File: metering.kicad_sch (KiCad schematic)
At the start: 6 parts, among them J1 Electric Meter IR TTL, J2 Gas Meter Reed Contact, U1 NodeMCU v2

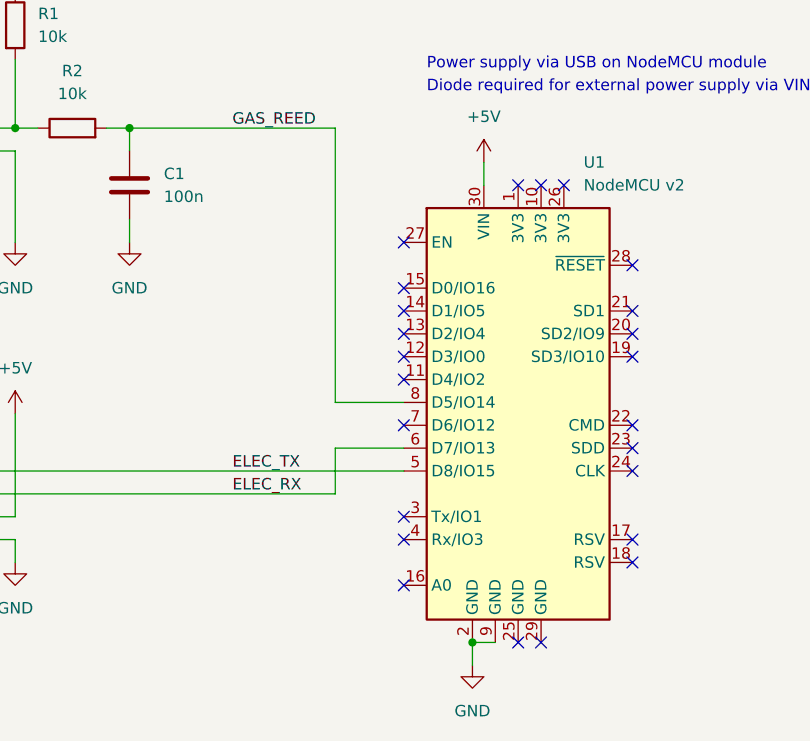
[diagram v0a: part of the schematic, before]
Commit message: Update power symbols, add power flags to satisfy ERC
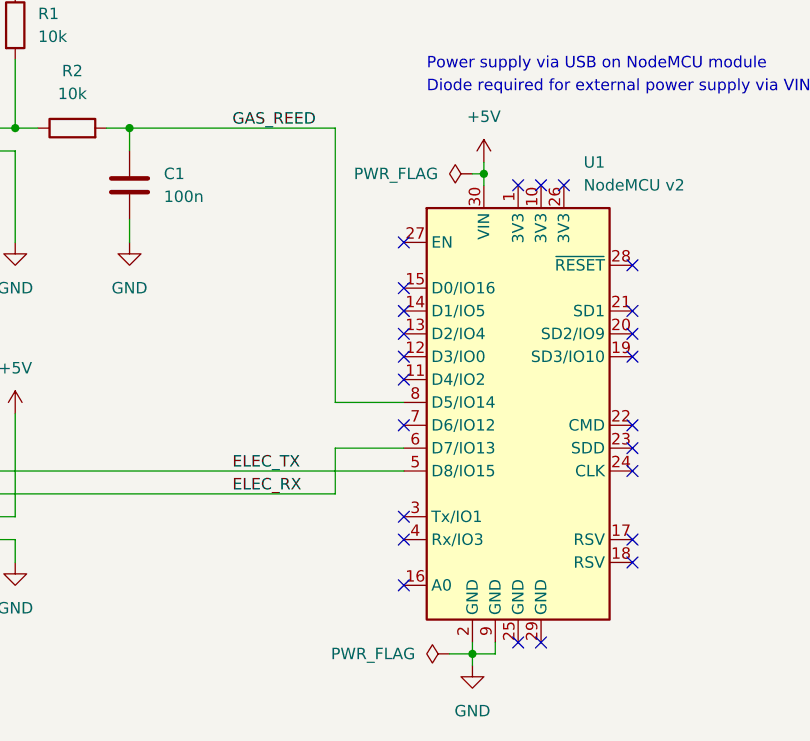
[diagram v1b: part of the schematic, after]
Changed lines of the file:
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@@
+	)
+	(junction
+		(at 139.7 109.22)
+		(diameter 0)
+		(color 0 0 0 0)
+	)
+	(junction
+		(at 140.97 55.88)
+		(diameter 0)
+		(color 0 0 0 0)
 	)
 	(junction
@@
 		(color 0 0 0 0)
 	)
-	(junction
-		(at 139.7 107.95)
-		(diameter 0)
-		(color 0 0 0 0)
-	)
 	(no_connect
 		(at 132.08 76.2)
@@
 	(wire
 		(pts
+			(xy 139.7 109.22) (xy 139.7 107.95)
+		)
+		(stroke
+			(width 0)
+			(type default)
+		)
+	)
+	(wire
+		(pts
 			(xy 88.9 50.8) (xy 91.44 50.8)
 		)
@@
 	(wire
 		(pts
+			(xy 139.7 109.22) (xy 139.7 110.49)
+		)
+		(stroke
+			(width 0)
+			(type default)
+		)
+	)
+	(wire
+		(pts
 			(xy 88.9 33.02) (xy 88.9 35.56)
 		)
@@
 	(wire
 		(pts
+			(xy 137.16 109.22) (xy 139.7 109.22)
+		)
+		(stroke
+			(width 0)
+			(type default)
+		)
+	)
+	(wire
+		(pts
 			(xy 81.28 50.8) (xy 88.9 50.8)
 		)
@@
 	(wire
 		(pts
+			(xy 142.24 109.22) (xy 142.24 107.95)
+		)
+		(stroke
+			(width 0)
+			(type default)
+		)
+	)
+	(wire
+		(pts
 			(xy 88.9 43.18) (xy 88.9 50.8)
 		)
@@
 	(wire
 		(pts
-			(xy 140.97 57.15) (xy 140.97 54.61)
+			(xy 140.97 55.88) (xy 140.97 54.61)
+		)
+		(stroke
+			(width 0)
+			(type default)
+		)
+	)
+	(wire
+		(pts
+			(xy 140.97 57.15) (xy 140.97 55.88)
 		)
 		(stroke
@@
 	(wire
 		(pts
-			(xy 139.7 107.95) (xy 139.7 110.49)
-		)
-		(stroke
-			(width 0)
-			(type default)
-		)
-	)
-	(wire
-		(pts
 			(xy 88.9 53.34) (xy 81.28 53.34)
 		)
@@
 	(wire
 		(pts
-			(xy 139.7 107.95) (xy 142.24 107.95)
+			(xy 139.7 55.88) (xy 140.97 55.88)
+		)
+		(stroke
+			(width 0)
+			(type default)
+		)
+	)
+	(wire
+		(pts
+			(xy 139.7 109.22) (xy 142.24 109.22)
 		)
 		(stroke
@@
 			)
 			(justify left bottom)
+		)
+	)
+	(symbol
+		(lib_id "power:PWR_FLAG")
+		(at 139.7 55.88 90)
+		(unit 1)
+		(exclude_from_sim no)
+		(in_bom yes)
+		(on_board yes)
+		(dnp no)
+		(fields_autoplaced yes)
+		(property "Reference" "#FLG01"
+			(at 137.795 55.88 0)
+			(effects
+				(font
+					(size 1.27 1.27)
+				)
+				(hide yes)
+			)
+		)
+		(property "Value" "PWR_FLAG"
+			(at 135.89 55.8799 90)
+			(effects
+				(font
+					(size 1.27 1.27)
+				)
+				(justify left)
+			)
+		)
+		(property "Footprint" ""
+			(at 139.7 55.88 0)
+			(effects
+				(font
+					(size 1.27 1.27)
+				)
+				(hide yes)
+			)
+		)
+		(property "Datasheet" "~"
+			(at 139.7 55.88 0)
+			(effects
+				(font
+					(size 1.27 1.27)
+				)
+				(hide yes)
+			)
+		)
+		(property "Description" "Special symbol for telling ERC where power comes from"
+			(at 139.7 55.88 0)
+			(effects
+				(font
+					(size 1.27 1.27)
+				)
+				(hide yes)
+			)
+		)
+		(pin "1"
+		)
+		(instances
+			(project ""
+				(path "/2132c704-8b90-4a68-a04d-0b4be367d67b"
+					(reference "#FLG01")
+					(unit 1)
+				)
+			)
 		)
 	)
@@
 			)
 		)
-		(property "Description" ""
+		(property "Description" "Power symbol creates a global label with name \"+5V\""
 			(at 140.97 54.61 0)
 			(effects
@@
 			)
 		)
-		(property "Description" ""
+		(property "Description" "Power symbol creates a global label with name \"GND\" , ground"
 			(at 139.7 110.49 0)
 			(effects
@@
 	)
 	(symbol
+		(lib_id "power:PWR_FLAG")
+		(at 137.16 109.22 90)
+		(unit 1)
+		(exclude_from_sim no)
+		(in_bom yes)
+		(on_board yes)
+		(dnp no)
+		(fields_autoplaced yes)
+		(property "Reference" "#FLG02"
+			(at 135.255 109.22 0)
+			(effects
+				(font
+					(size 1.27 1.27)
+				)
+				(hide yes)
+			)
+		)
+		(property "Value" "PWR_FLAG"
+			(at 133.35 109.2199 90)
+			(effects
+				(font
+					(size 1.27 1.27)
+				)
+				(justify left)
+			)
+		)
+		(property "Footprint" ""
+			(at 137.16 109.22 0)
+			(effects
+				(font
+					(size 1.27 1.27)
+				)
+				(hide yes)
+			)
+		)
+		(property "Datasheet" "~"
+			(at 137.16 109.22 0)
+			(effects
+				(font
+					(size 1.27 1.27)
+				)
+				(hide yes)
+			)
+		)
+		(property "Description" "Special symbol for telling ERC where power comes from"
+			(at 137.16 109.22 0)
+			(effects
+				(font
+					(size 1.27 1.27)
+				)
+				(hide yes)
+			)
+		)
+		(pin "1"
+		)
+		(instances
+			(project "metering"
+				(path "/2132c704-8b90-4a68-a04d-0b4be367d67b"
+					(reference "#FLG02")
+					(unit 1)
+				)
+			)
+		)
+	)
+	(symbol
 		(lib_id "power:GND")
 		(at 88.9 63.5 0)
@@
 			)
 		)
-		(property "Description" ""
+		(property "Description" "Power symbol creates a global label with name \"GND\" , ground"
 			(at 88.9 63.5 0)
 			(effects
@@
 			)
 		)
-		(property "Description" ""
+		(property "Description" "Power symbol creates a global label with name \"+5V\""
 			(at 88.9 33.02 0)
 			(effects
@@
 			)
 		)
-		(property "Description" ""
+		(property "Description" "Power symbol creates a global label with name \"GND\" , ground"
 			(at 88.9 99.06 0)
 			(effects
@@
 			)
 		)
-		(property "Description" ""
+		(property "Description" "Power symbol creates a global label with name \"GND\" , ground"
 			(at 101.6 63.5 0)
 			(effects
@@
 			)
 		)
-		(property "Description" ""
+		(property "Description" "Power symbol creates a global label with name \"+5V\""
 			(at 88.9 82.55 0)
 			(effects

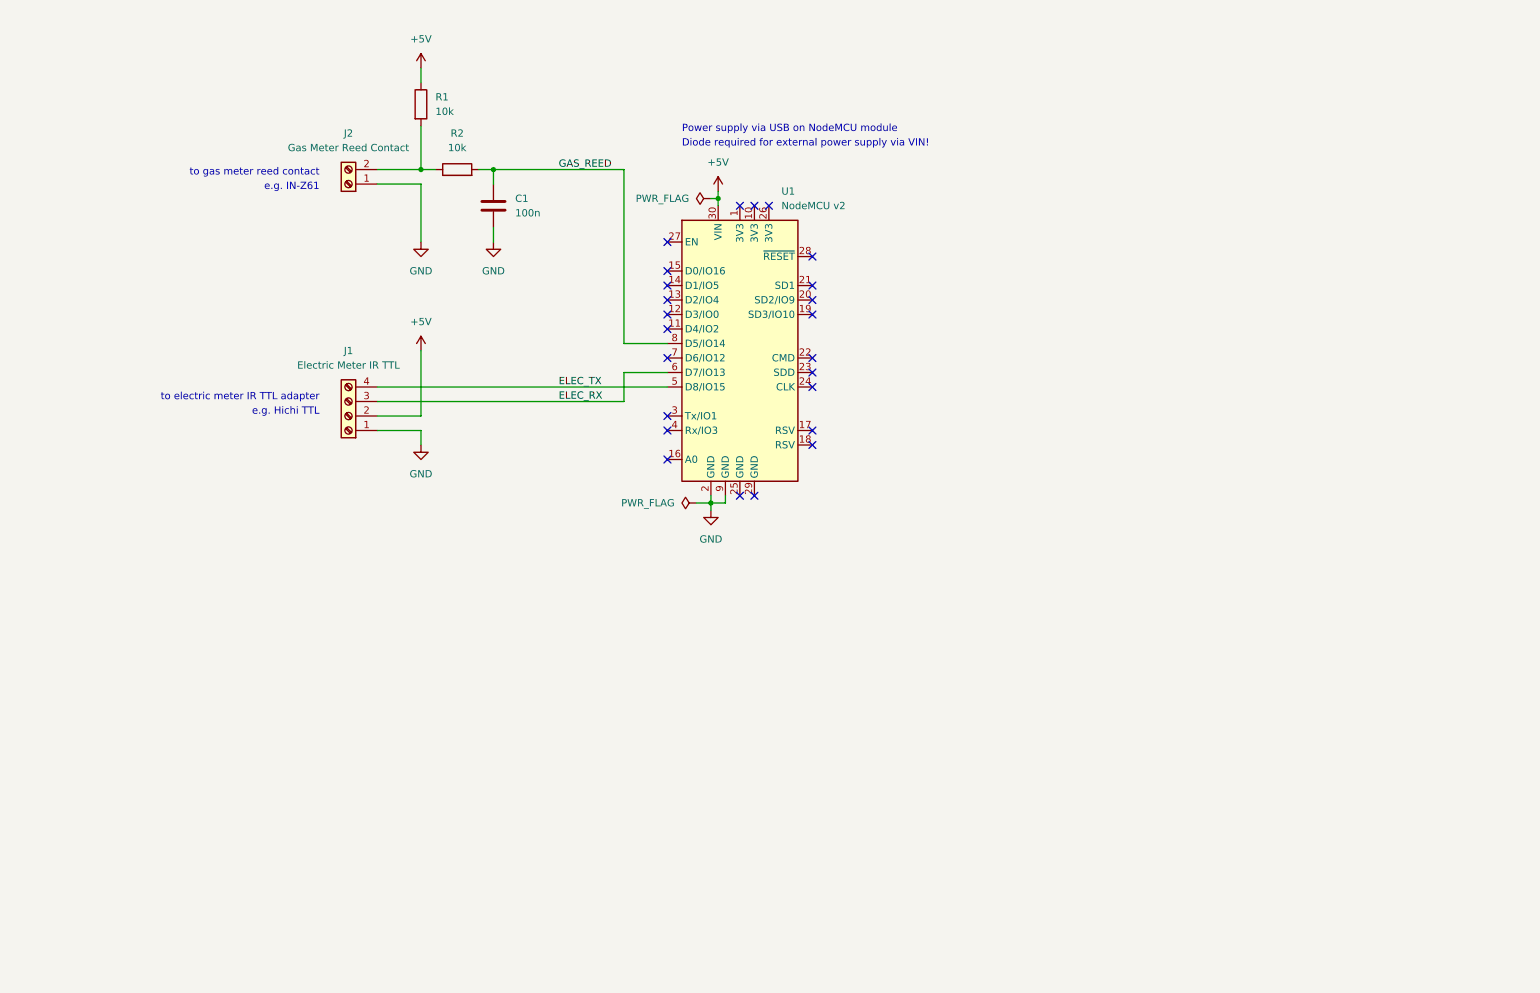
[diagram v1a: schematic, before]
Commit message: Recreate schematic with ESP32-C3-WROOM module and hardware debounce
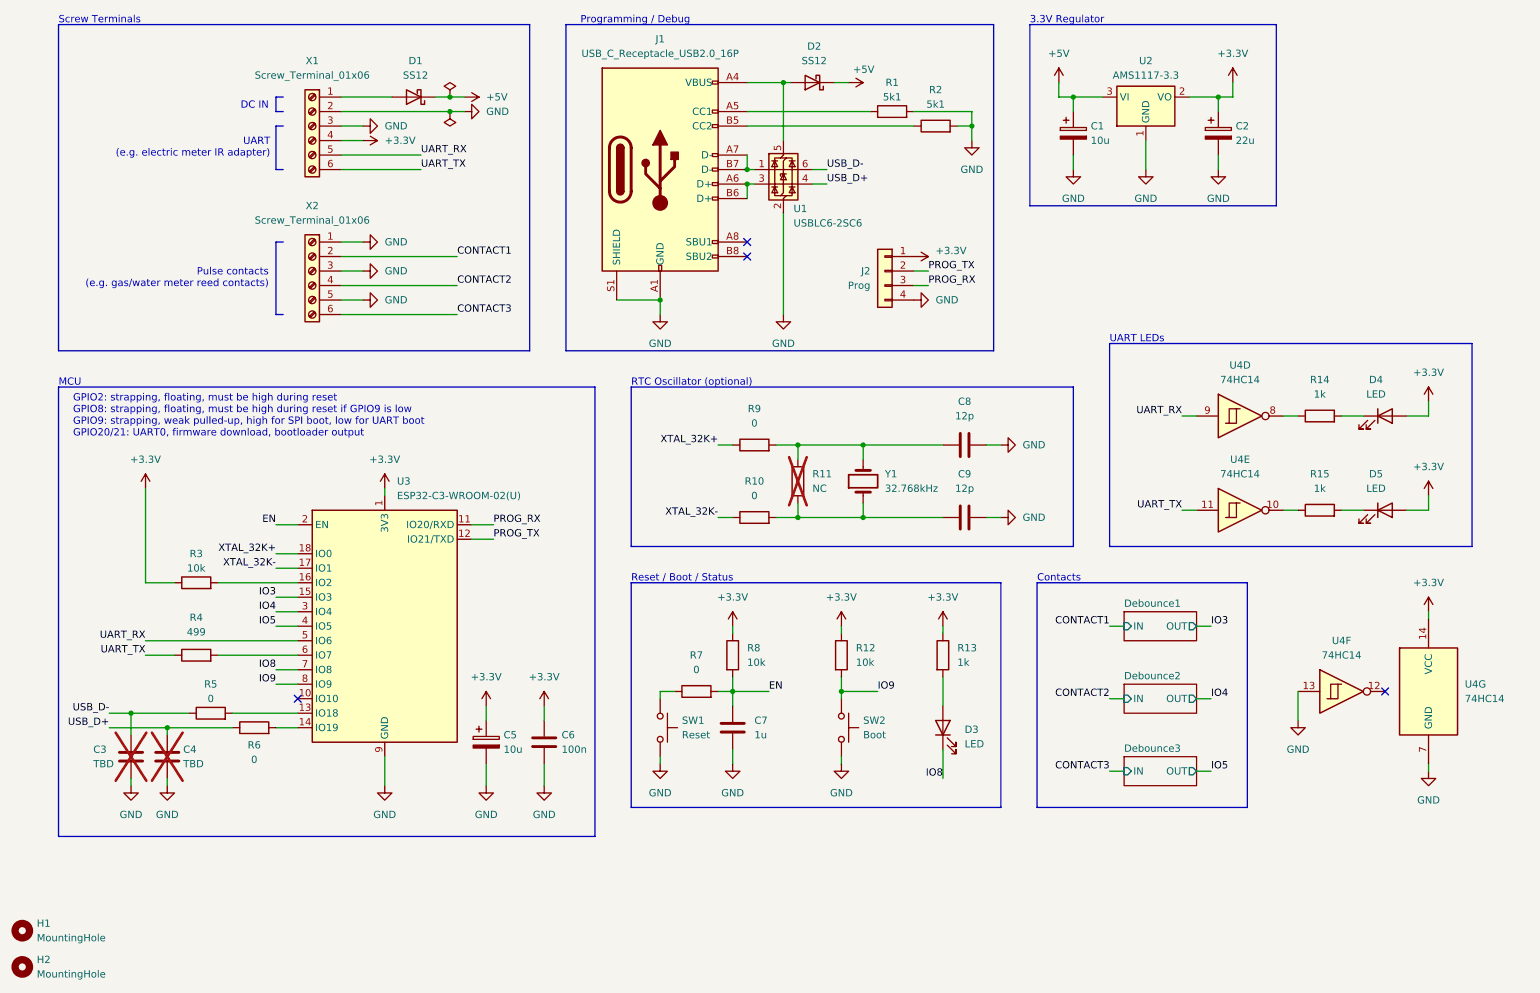
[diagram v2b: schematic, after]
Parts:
- removed C1: 100n, symbol Device:C
- removed J1: Electric Meter IR TTL, Connector_PinSocket_2.54mm:PinSocket_1x04_P2.54mm_Vertical, symbol Connector:Screw_Terminal_01x04
- removed J2: Gas Meter Reed Contact, Connector_PinSocket_2.54mm:PinSocket_1x02_P2.54mm_Vertical, symbol Connector:Screw_Terminal_01x02
- removed U1: NodeMCU v2, NodeMCU_v2:NodeMCU_v2, symbol NodeMCU_v2:NodeMCU_v2
- added C1, C5: 10u, Capacitor_Tantalum_SMD:CP_EIA-3216-18_Kemet-A, symbol Device:C_Polarized
- added C2: 22u, Capacitor_Tantalum_SMD:CP_EIA-3216-18_Kemet-A, symbol Device:C_Polarized
- added C3, C4: TBD, Capacitor_SMD:C_0805_2012Metric, symbol Device:C
- added C6: 100n, Capacitor_SMD:C_0805_2012Metric, symbol Device:C
- added C7: 1u, Capacitor_SMD:C_0805_2012Metric, symbol Device:C
- added C8, C9: 12p, Capacitor_SMD:C_0805_2012Metric, symbol Device:C
- added D1, D2: SS12, Diode_SMD:D_SMA, symbol Diode:SS12
- added D3, D4, D5: LED, LED_THT:LED_D3.0mm_Horizontal_O6.35mm_Z2.0mm, symbol Device:LED
- added H1, H2: MountingHole, MountingHole:MountingHole_3.2mm_M3, symbol Mechanical:MountingHole
- added J1: USB_C_Receptacle_USB2.0_16P, Connector_USB:USB_C_Receptacle_GCT_USB4110, symbol Connector:USB_C_Receptacle_USB2.0_16P
- added J2: Prog, Connector_PinHeader_2.54mm:PinHeader_1x04_P2.54mm_Vertical, symbol Connector_Generic:Conn_01x04
- added R10, R5, R6, R7, R9: 0, Resistor_SMD:R_0805_2012Metric, symbol Device:R
- added R11: NC, Resistor_SMD:R_0805_2012Metric, symbol Device:R
- added R12, R3, R8: 10k, Resistor_SMD:R_0805_2012Metric, symbol Device:R
- added R13, R14, R15: 1k, Resistor_SMD:R_0805_2012Metric, symbol Device:R
- added R4: 499, Resistor_SMD:R_0805_2012Metric, symbol Device:R
- added SW1: Reset, Button_Switch_SMD:SW_SPST_PTS647_Sx38, symbol Switch:SW_Push
- added SW2: Boot, Button_Switch_SMD:SW_SPST_PTS647_Sx38, symbol Switch:SW_Push
- added U1: USBLC6-2SC6, Package_TO_SOT_SMD:SOT-23-6, symbol Power_Protection:USBLC6-2SC6
- added U2: AMS1117-3.3, Package_TO_SOT_SMD:SOT-223-3_TabPin2, symbol Regulator_Linear:AMS1117-3.3
- added U3: ESP32-C3-WROOM-02(U), RF_Module:ESP32-C3-WROOM-02, symbol RF_Module:ESP32-C3-WROOM-02
- added U4: 74HC14, Package_SO:SOIC-14_3.9x8.7mm_P1.27mm, symbol 74xx:74HC14
- added X1, X2: Screw_Terminal_01x06, TerminalBlock_Phoenix:TerminalBlock_Phoenix_MKDS-1,5-6-5.08_1x06_P5.08mm_Horizontal, symbol Connector:Screw_Terminal_01x06
- added Y1: 32.768kHz, Crystal:Crystal_SMD_3215-2Pin_3.2x1.5mm, symbol Device:Crystal
- R1, R2: value 10k -> 5k1; footprint (none) -> Resistor_SMD:R_0805_2012Metric
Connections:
- net GAS_REED is gone; now on net GND: R2.2
- net +5V: now also C1.1, D1.1 (K), D2.1 (K), U2.3 (VI); no longer R1.1
- net GND: now also R1.2, C1.2, C2.2, C3.2, C4.2, C5.2, C6.2, C7.2, C8.2, C9.2, J1.A1 (GND), J1.A12 (GND), J1.B1 (GND), J1.B12 (GND), J1.S1 (SHIELD), J2.4 (Pin_4), SW1.2, SW2.2, U1.2 (GND), U2.1 (GND), U3.19 (GND), U3.9 (GND), U4.13, U4.7 (GND), X1.2 (Pin_2), X1.3 (Pin_3), X2.1 (Pin_1), X2.3 (Pin_3), X2.5 (Pin_5)
- net at R2.1: now also J1.B5 (CC2); no longer R1.2
- new net: R14.1, U4.8
- new net: R7.1, SW1.1
- new net: R15.1, U4.10
- new net: C8.1, R11.2, R9.2, Y1.2
- new net: R3.2, U3.16 (IO2)
- new net: R6.2, U3.14 (IO19)
- new net: C9.1, R10.2, R11.1, Y1.1
- new net: D3.2 (A), R13.2
- new net: J1.A5 (CC1), R1.1
- new net: D5.1 (K), R15.2
- new net: R5.2, U3.13 (IO18)
- new net: D2.2 (A), J1.A4 (VBUS), J1.A9 (VBUS), J1.B4 (VBUS), J1.B9 (VBUS), U1.5 (VBUS)
- new net: J1.A7 (D-), J1.B7 (D-), U1.1 (I/O1)
- new net: J1.A6 (D+), J1.B6 (D+), U1.3 (I/O2)
- new net: D1.2 (A), X1.1 (Pin_1)
- new net: D4.1 (K), R14.2
- new net: R4.2, U3.6 (IO7)
- new net +3.3V: C2.1, C5.1, C6.1, D4.2 (A), D5.2 (A), J2.1 (Pin_1), R12.1, R13.1, R3.1, R8.1, U2.2 (VO), U3.1 (3V3), U4.14 (VCC), X1.4 (Pin_4)
- new net CONTACT1: X2.2 (Pin_2)
- new net CONTACT2: X2.4 (Pin_4)
- new net CONTACT3: X2.6 (Pin_6)
- new net EN: C7.1, R7.2, R8.2, U3.2 (EN)
- new net IO3: U3.15 (IO3)
- new net IO4: U3.3 (IO4)
- new net IO5: U3.4 (IO5)
- new net IO8: D3.1 (K), U3.7 (IO8)
- new net IO9: R12.2, SW2.1, U3.8 (IO9)
- new net PROG_RX: J2.3 (Pin_3), U3.11 (IO20/RXD)
- new net PROG_TX: J2.2 (Pin_2), U3.12 (IO21/TXD)
- new net UART_RX: U3.5 (IO6), U4.9, X1.5 (Pin_5)
- new net UART_TX: R4.1, U4.11, X1.6 (Pin_6)
- new net USB_D+: C4.1, R6.1, U1.4 (I/O2)
- new net USB_D-: C3.1, R5.1, U1.6 (I/O1)
- new net XTAL_32K+: R9.1, U3.18 (IO0)
- new net XTAL_32K-: R10.1, U3.17 (IO1)
- no-connect marks 24 -> 4
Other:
- added sheet Debounce1 (debounce.kicad_sch)
- added sheet Debounce2 (debounce.kicad_sch)
- added sheet Debounce3 (debounce.kicad_sch)
- note added: "3.3V Regulator"
- note added: "Contacts"
- note added: "DC IN"
- note added: "GPIO2: strapping, floating, must be high during reset GPIO8: strapping, floating, must be high during reset if GPIO9 is low GPIO9: strapping, weak pulled-up, high for SPI boot, low for UART boot GPIO20/21: UART0, firmware download, bootloader output"
- note added: "MCU"
- note added: "Programming / Debug"
- note added: "Pulse contacts (e.g. gas/water meter reed contacts)"
- note added: "RTC Oscillator (optional)"
- note added: "Reset / Boot / Status"
- note added: "Screw Terminals"
- note added: "UART (e.g. electric meter IR adapter)"
- note added: "UART LEDs"
- note removed: "Diode required for external power supply via VIN!"
- note removed: "Power supply via USB on NodeMCU module"
- note removed: "e.g. Hichi TTL"
- note removed: "e.g. IN-Z61"
- note removed: "to electric meter IR TTL adapter"
- note removed: "to gas meter reed contact"

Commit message: Adjust some footprints and PCB settings
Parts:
- D3, D4, D5: footprint LED_THT:LED_D3.0mm_Horizontal_O6.35mm_Z2.0mm -> LED_THT:LED_D3.0mm_Horizontal_O3.81mm_Z2.0mm
- U3: value ESP32-C3-WROOM-02(U) -> ESP32-C3-WROOM-02U; footprint RF_Module:ESP32-C3-WROOM-02 -> RF_Module:ESP32-C3-WROOM-02U
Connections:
- net VBUS: now reaches D2.2 (A), J1.A4 (VBUS), J1.A9 (VBUS), J1.B4 (VBUS), J1.B9 (VBUS), U1.5 (VBUS)
- net VIN: now reaches D1.2 (A), X1.1 (Pin_1)
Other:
- note added: "IO2: strapping, floating, must be high during reset IO8: strapping, floating, must be high during reset if GPIO9 is low IO9: strapping, weak pulled-up, high for SPI boot, low for UART boot IO20/21: UART0, firmware download, bootloader output"
- note removed: "GPIO2: strapping, floating, must be high during reset GPIO8: strapping, floating, must be high during reset if GPIO9 is low GPIO9: strapping, weak pulled-up, high for SPI boot, low for UART boot GPIO20/21: UART0, firmware download, bootloader output"
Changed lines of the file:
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@@
 	(title_block
 		(title "Smart Home Energy Metering")
-		(date "2025-06-10")
+		(date "2025-06-15")
 		(rev "1.0")
 		(comment 1 "https://github.com/zargony/smarthome-metering")
@@
 		)
 	)
-	(text "GPIO2: strapping, floating, must be high during reset\nGPIO8: strapping, floating, must be high during reset if GPIO9 is low\nGPIO9: strapping, weak pulled-up, high for SPI boot, low for UART boot\nGPIO20/21: UART0, firmware download, bootloader output"
+	(text "IO2: strapping, floating, must be high during reset\nIO8: strapping, floating, must be high during reset if GPIO9 is low\nIO9: strapping, weak pulled-up, high for SPI boot, low for UART boot\nIO20/21: UART0, firmware download, bootloader output"
 		(exclude_from_sim no)
 		(at 27.94 93.98 0)
@@
 		)
 	)
+	(label "VIN"
+		(at 76.2 38.1 0)
+		(effects
+			(font
+				(size 1.27 1.27)
+			)
+			(justify left bottom)
+		)
+	)
 	(label "IO5"
 		(at 63.5 130.81 180)
@@
 		)
 	)
+	(label "VBUS"
+		(at 147.32 35.56 0)
+		(effects
+			(font
+				(size 1.27 1.27)
+			)
+			(justify left bottom)
+		)
+	)
 	(label "UART_TX"
 		(at 40.64 135.89 180)
@@
 			)
 		)
-		(property "Footprint" "LED_THT:LED_D3.0mm_Horizontal_O6.35mm_Z2.0mm"
+		(property "Footprint" "LED_THT:LED_D3.0mm_Horizontal_O3.81mm_Z2.0mm"
 			(at 180.34 148.59 0)
 			(effects
@@
 			)
 		)
-		(property "Value" "ESP32-C3-WROOM-02(U)"
+		(property "Value" "ESP32-C3-WROOM-02U"
 			(at 84.6933 107.95 0)
 			(effects
@@
 			)
 		)
-		(property "Footprint" "RF_Module:ESP32-C3-WROOM-02"
+		(property "Footprint" "RF_Module:ESP32-C3-WROOM-02U"
 			(at 82.55 130.175 0)
 			(effects
@@
 			)
 		)
-		(property "Footprint" "LED_THT:LED_D3.0mm_Horizontal_O6.35mm_Z2.0mm"
+		(property "Footprint" "LED_THT:LED_D3.0mm_Horizontal_O3.81mm_Z2.0mm"
 			(at 257.81 93.98 0)
 			(effects
@@
 			)
 		)
-		(property "Footprint" "LED_THT:LED_D3.0mm_Horizontal_O6.35mm_Z2.0mm"
+		(property "Footprint" "LED_THT:LED_D3.0mm_Horizontal_O3.81mm_Z2.0mm"
 			(at 257.81 110.49 0)
 			(effects
